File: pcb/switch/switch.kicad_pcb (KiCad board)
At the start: 2 copper layers, 70.5 x 70.5 mm, 31 parts, among them J1 Conn_01x06, J2 Conn_01x04, J3 Conn_01x05, J4 Conn_01x04, K1 G6SU-2, K2 G6SU-2, K3 G6SU-2, K4 G6SU-2, SW1 D2F-01, SW2 D2F-01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

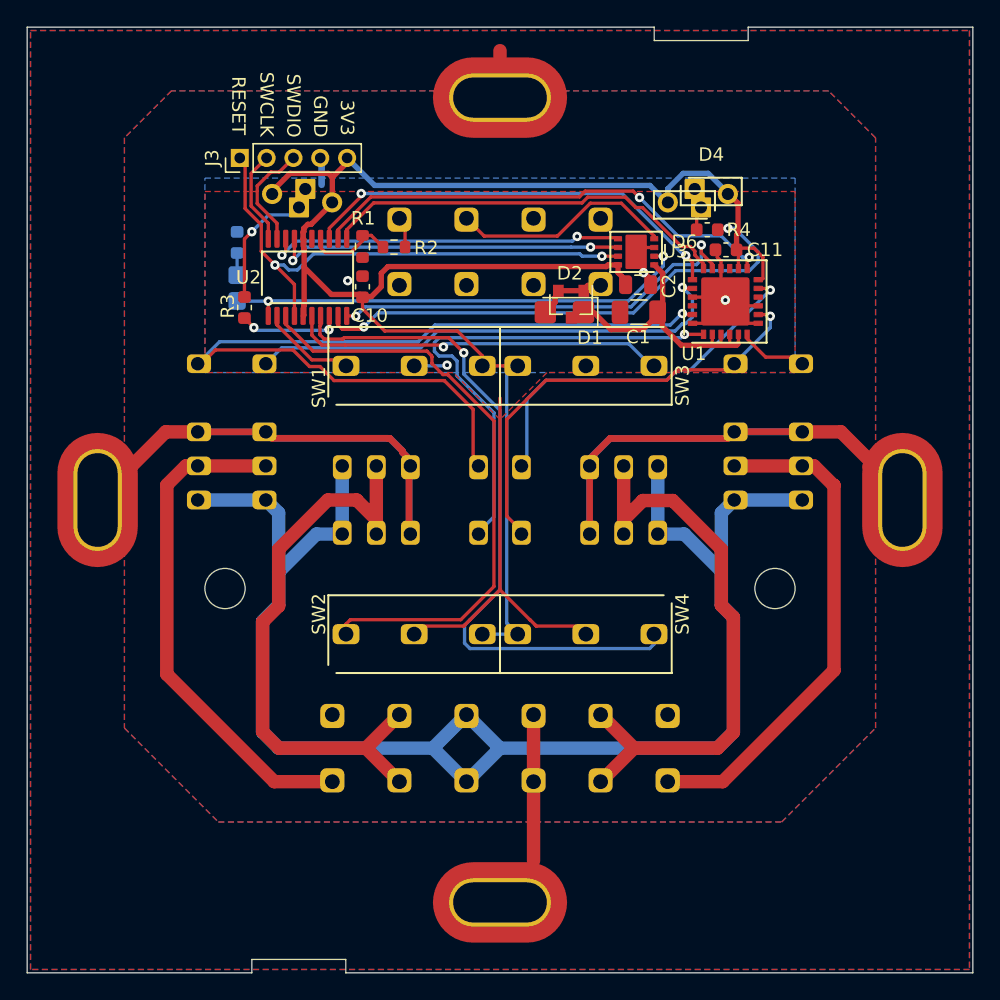
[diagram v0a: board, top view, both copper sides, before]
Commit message: First prototype of PCB and switch to KiCad 6 (#25)
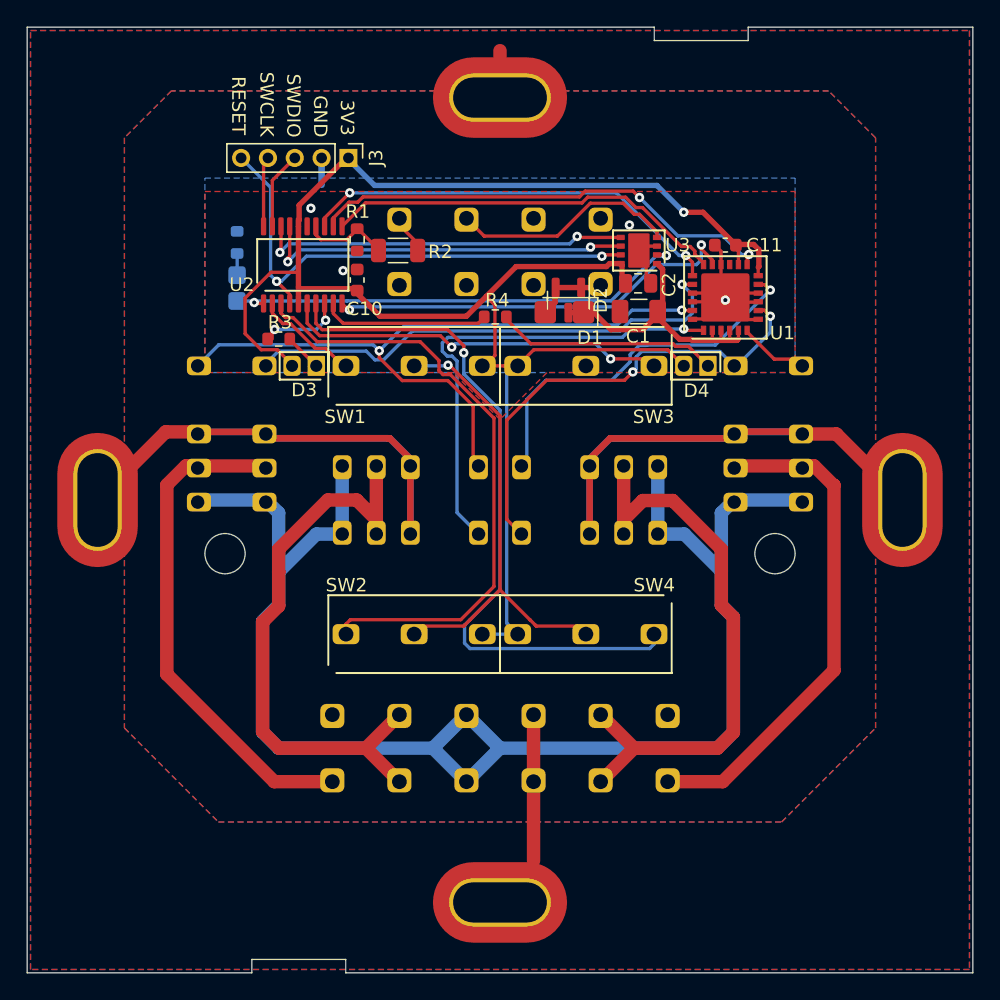
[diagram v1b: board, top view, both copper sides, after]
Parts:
- removed D5, D6: LED, RoomControl:DiodeHolesR
- D2: value D_Schottky_x2_KCom_AAK -> BAS40-05/BAT54C
- D3: footprint RoomControl:DiodeHolesR -> RoomControl:DiodeHolesSwitch; moved to F.Cu
- D4: footprint RoomControl:DiodeHolesR -> RoomControl:DiodeHolesSwitch
- R2: footprint Resistor_SMD:R_0603_1608Metric -> Resistor_SMD:R_1206_3216Metric
- moved R4 17.1 mm to (99.7, 86.3), turned to 180 degrees
- moved D3 13.1 mm to (85.4, 90.0)
- moved D4 13.1 mm to (114.6, 90.0), turned to 180 degrees
- moved J3 8.10 mm to (88.7, 74.5), turned to -90 degrees
- moved R3 3.47 mm to (83.5, 88.0), turned to 180 degrees
- moved U2 0.99 mm to (85.3, 82.5)
- moved C10 0.64 mm to (89.3, 83.6)
- moved R1 0.64 mm to (89.3, 80.6)
- moved R2 0.39 mm to (92.4, 81.4)
- moved D2 0.36 mm to (105.1, 85.1)
- moved C11 0.35 mm to (116.8, 81.0)
- moved U1 0.30 mm to (116.8, 84.9)
- moved U3 0.22 mm to (110.3, 81.4)
- moved K2 0.16 mm to (80.0, 90.0)
- moved K4 0.16 mm to (120.0, 90.0)
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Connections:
- J3 pad 1: RESET -> +3V3
- J3 pad 2: SWCLK -> GND
- J3 pad 4: GND -> SWCLK
- J3 pad 5: +3V3 -> RESET
- U1 pad 15: Net-(U1-Pad15) -> unconnected-(U1-Pad15)
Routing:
- net LEDB: track 38.7 -> 12.9 mm, vias 2 -> 0
- net Net-(D4-Pad1): track 3.10 -> 16.7 mm
- net AY: track 65.7 -> 52.9 mm, vias 1 -> 2
- net GND: track 46.7 -> 57.8 mm, vias 4 -> 5
- net +3V3: track 127.5 -> 135.1 mm, vias 0 -> 1
- net PE: track 130.1 -> 122.7 mm
- net Net-(D3-Pad1): track 10.8 -> 3.49 mm, vias 1 -> 0
- net SWDIO: track 8.12 -> 5.79 mm
- net AX: track 37.5 -> 35.5 mm
- net SWCLK: track 7.03 -> 5.23 mm
- net +12V: track 21.6 -> 19.8 mm
- net BY: track 33.3 -> 35.0 mm, vias 1 -> 2
- net BUS_TX: track 26.4 -> 28.0 mm
- net LEDA: track 7.77 -> 6.16 mm
- net SWA0: track 7.30 -> 8.85 mm
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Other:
- net class Default removed
- net class Mains removed
